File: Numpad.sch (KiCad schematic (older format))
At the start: 7 parts, among them U16 SN74LVC1G04DBVR, U17 74LS597, U18 74LS597, U19 74LS597

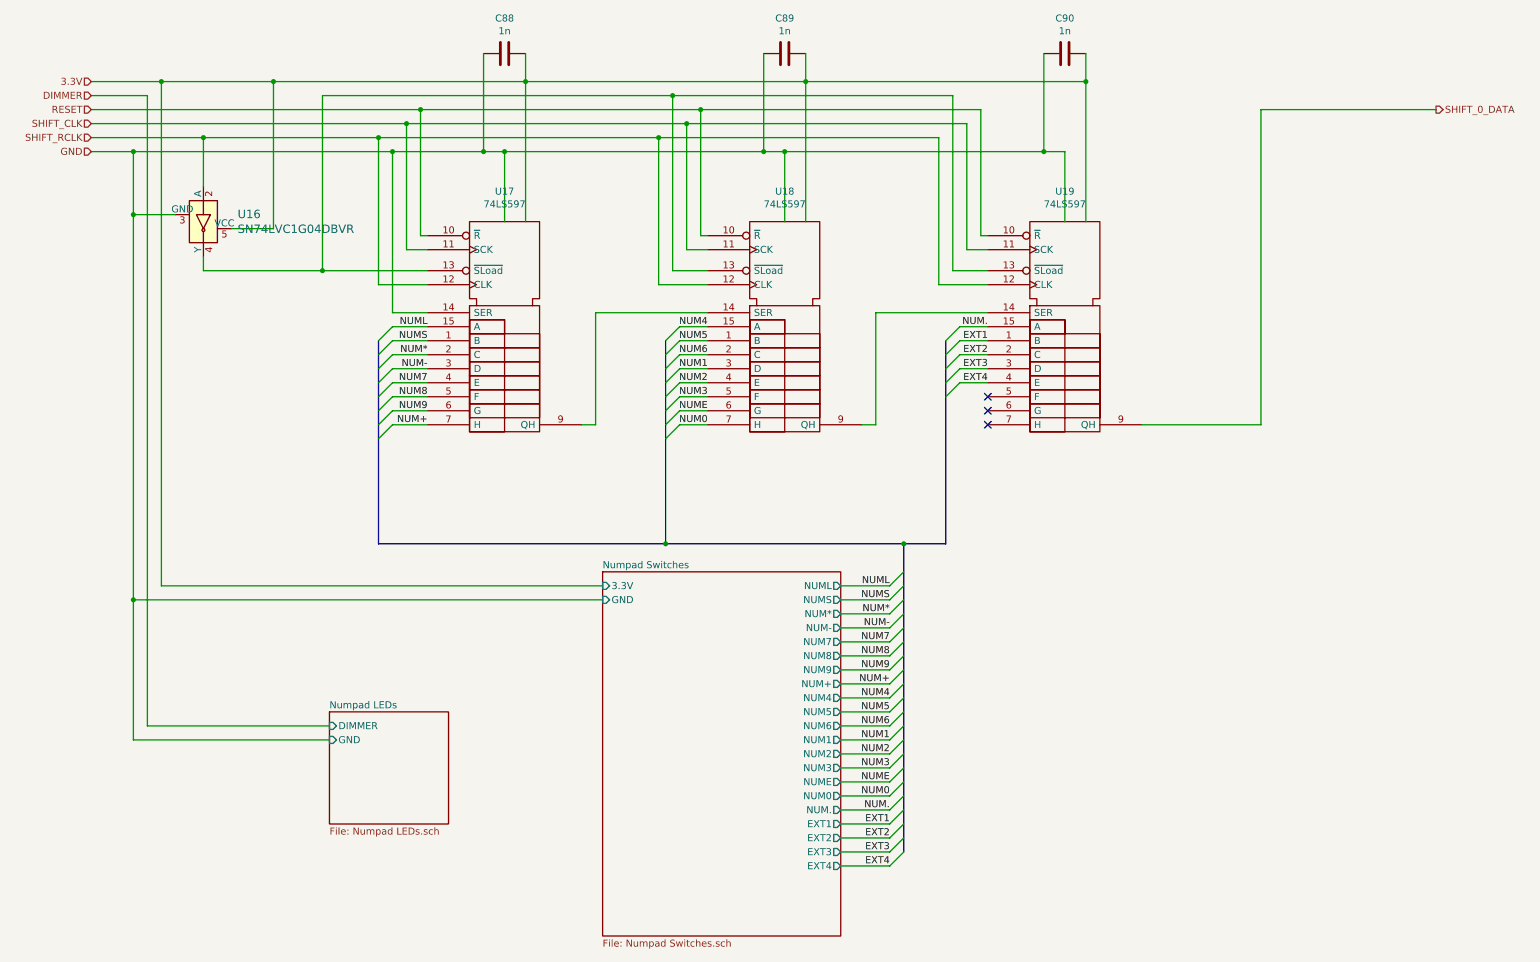
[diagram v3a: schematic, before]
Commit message: Redesigned for single large PCB
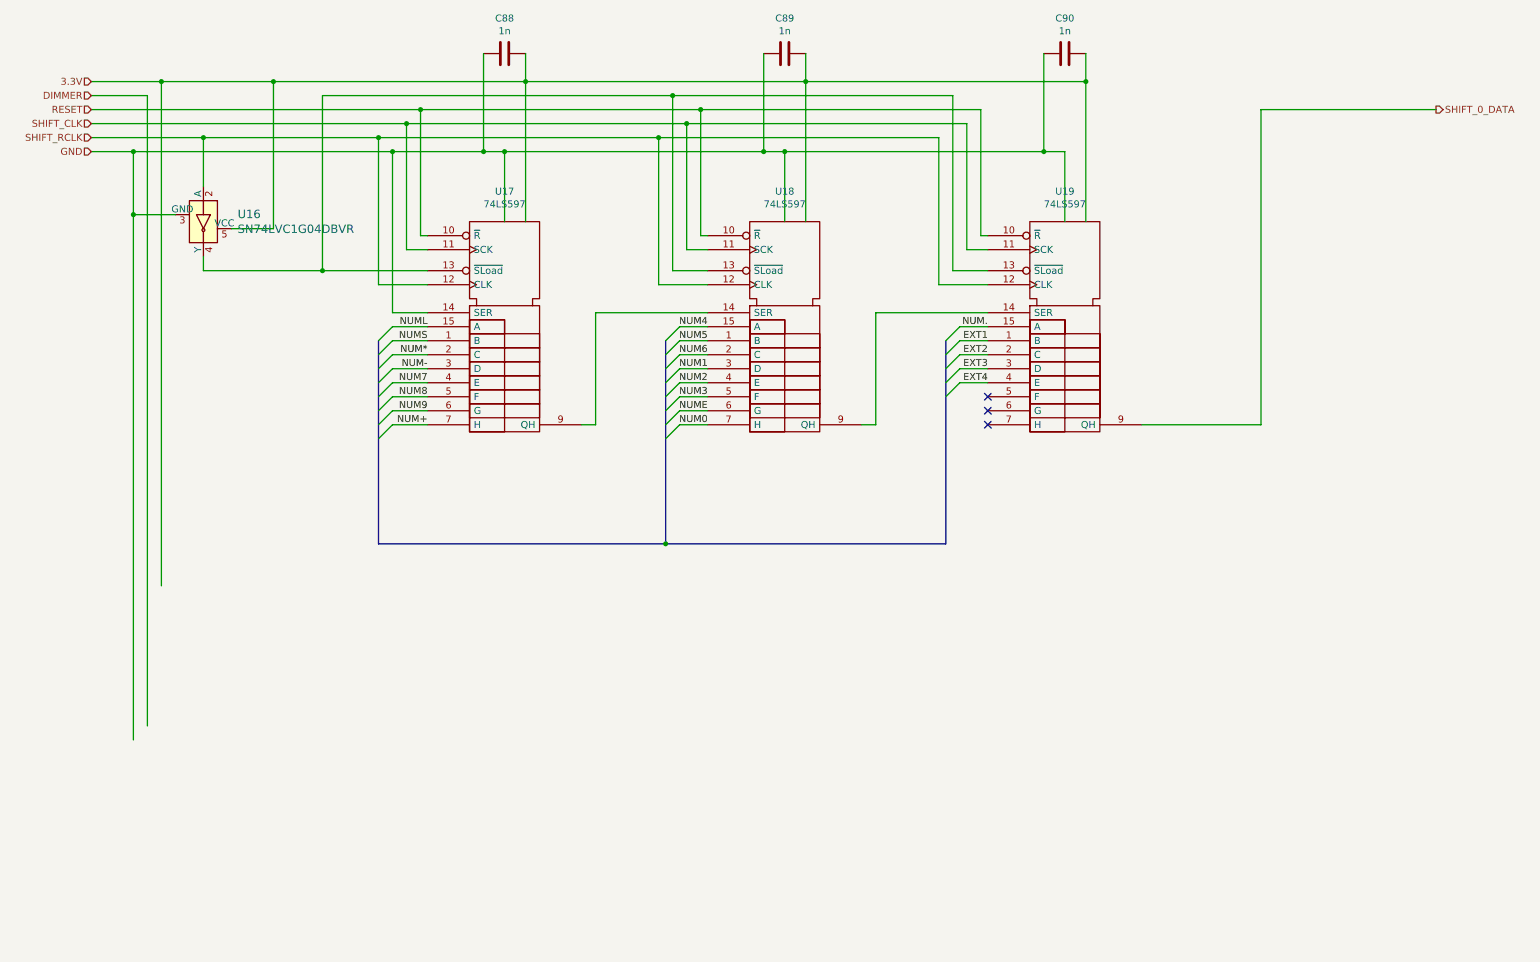
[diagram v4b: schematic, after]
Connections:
- wire segments 130 -> 104
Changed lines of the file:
@@
 $Descr A4 11693 8268
 encoding utf-8
-Sheet 13 18
+Sheet 18 18
 Title ""
 Date ""
@@
 	1400 1200 1400 5700
 Wire Wire Line
-	1400 5700 2700 5700
-Wire Wire Line
 	1500 1100 1500 4700
-Wire Wire Line
-	1300 5800 2700 5800
 Wire Wire Line
 	9350 1300 9350 3550
@@
 Wire Wire Line
 	1300 1600 1300 2050
-Wire Wire Line
-	4650 4800 1300 4800
-Connection ~ 1300 4800
-Wire Wire Line
-	1300 4800 1300 5800
-Wire Wire Line
-	1500 4700 4650 4700
 Wire Wire Line
 	7200 2850 7400 2850
@@
 Entry Wire Line
 	7100 3350 7200 3250
-$Sheet
-S 4650 4600 1700 2600
-U 5E9CBBD2
-F0 "Numpad Switches" 50
-F1 "Numpad Switches.sch" 50
-F2 "3.3V" I L 4650 4700 50
-F3 "GND" I L 4650 4800 50
-F4 "NUML" O R 6350 4700 50
-F5 "NUMS" O R 6350 4800 50
-F6 "NUM*" O R 6350 4900 50
-F7 "NUM-" O R 6350 5000 50
-F8 "NUM7" O R 6350 5100 50
-F9 "NUM8" O R 6350 5200 50
-F10 "NUM9" O R 6350 5300 50
-F11 "NUM+" O R 6350 5400 50
-F12 "NUM4" O R 6350 5500 50
-F13 "NUM5" O R 6350 5600 50
-F14 "NUM6" O R 6350 5700 50
-F15 "NUM1" O R 6350 5800 50
-F16 "NUM2" O R 6350 5900 50
-F17 "NUM3" O R 6350 6000 50
-F18 "NUME" O R 6350 6100 50
-F19 "NUM0" O R 6350 6200 50
-F20 "NUM." O R 6350 6300 50
-F21 "EXT1" O R 6350 6400 50
-F22 "EXT2" O R 6350 6500 50
-F23 "EXT3" O R 6350 6600 50
-F24 "EXT4" O R 6350 6700 50
-$EndSheet
-Wire Wire Line
-	6350 4700 6700 4700
-Wire Wire Line
-	6350 4800 6700 4800
-Wire Wire Line
-	6350 4900 6700 4900
-Wire Wire Line
-	6350 5000 6700 5000
-Wire Wire Line
-	6350 5100 6700 5100
-Wire Wire Line
-	6350 5200 6700 5200
-Wire Wire Line
-	6350 5300 6700 5300
-Wire Wire Line
-	6350 5400 6700 5400
-Wire Wire Line
-	6350 5500 6700 5500
-Wire Wire Line
-	6350 5600 6700 5600
-Wire Wire Line
-	6350 5700 6700 5700
-Wire Wire Line
-	6350 5800 6700 5800
-Wire Wire Line
-	6350 5900 6700 5900
-Wire Wire Line
-	6350 6000 6700 6000
-Wire Wire Line
-	6350 6100 6700 6100
-Wire Wire Line
-	6350 6200 6700 6200
-Wire Wire Line
-	6350 6300 6700 6300
-Wire Wire Line
-	6350 6400 6700 6400
-Wire Wire Line
-	6350 6500 6700 6500
-Wire Wire Line
-	6350 6600 6700 6600
-Wire Wire Line
-	6350 6700 6700 6700
-Text Label 6700 4700 2    50   ~ 0
-NUML
-Text Label 6700 4800 2    50   ~ 0
-NUMS
-Text Label 6700 4900 2    50   ~ 0
-NUM*
-Text Label 6700 5000 2    50   ~ 0
-NUM-
-Text Label 6700 5100 2    50   ~ 0
-NUM7
-Text Label 6700 5200 2    50   ~ 0
-NUM8
-Text Label 6700 5300 2    50   ~ 0
-NUM9
-Text Label 6700 5400 2    50   ~ 0
-NUM+
-Text Label 6700 5500 2    50   ~ 0
-NUM4
-Text Label 6700 5600 2    50   ~ 0
-NUM5
-Text Label 6700 5700 2    50   ~ 0
-NUM6
-Text Label 6700 5800 2    50   ~ 0
-NUM1
-Text Label 6700 5900 2    50   ~ 0
-NUM2
-Text Label 6700 6000 2    50   ~ 0
-NUM3
-Text Label 6700 6100 2    50   ~ 0
-NUME
-Text Label 6700 6200 2    50   ~ 0
-NUM0
-Text Label 6700 6300 2    50   ~ 0
-NUM.
-Text Label 6700 6400 2    50   ~ 0
-EXT1
-Text Label 6700 6500 2    50   ~ 0
-EXT2
-Text Label 6700 6600 2    50   ~ 0
-EXT3
-Text Label 6700 6700 2    50   ~ 0
-EXT4
-Entry Wire Line
-	6700 4700 6800 4600
-Entry Wire Line
-	6700 4800 6800 4700
-Entry Wire Line
-	6700 4900 6800 4800
-Entry Wire Line
-	6700 5000 6800 4900
-Entry Wire Line
-	6700 5100 6800 5000
-Entry Wire Line
-	6700 5200 6800 5100
-Entry Wire Line
-	6700 5300 6800 5200
-Entry Wire Line
-	6700 5400 6800 5300
-Entry Wire Line
-	6700 5500 6800 5400
-Entry Wire Line
-	6700 5600 6800 5500
-Entry Wire Line
-	6700 5700 6800 5600
-Entry Wire Line
-	6700 5800 6800 5700
-Entry Wire Line
-	6700 5900 6800 5800
-Entry Wire Line
-	6700 6000 6800 5900
-Entry Wire Line
-	6700 6100 6800 6000
-Entry Wire Line
-	6700 6200 6800 6100
-Entry Wire Line
-	6700 6300 6800 6200
-Entry Wire Line
-	6700 6400 6800 6300
-Entry Wire Line
-	6700 6500 6800 6400
-Entry Wire Line
-	6700 6600 6800 6500
-Entry Wire Line
-	6700 6700 6800 6600
-Wire Bus Line
-	6800 4400 5100 4400
 Connection ~ 5100 4400
 Wire Bus Line
 	5100 4400 3050 4400
-Wire Bus Line
-	6800 4400 7100 4400
-Connection ~ 6800 4400
-$Sheet
-S 2700 5600 850  800
-U 5EFD9CB6
-F0 "Numpad LEDs" 50
-F1 "Numpad LEDs.sch" 50
-F2 "DIMMER" I L 2700 5700 50
-F3 "GND" I L 2700 5800 50
-$EndSheet
 $Comp
 L dk_Logic-Gates-and-Inverters:SN74LVC1G04DBVR U?
@@
 Connection ~ 1300 2050
 Wire Wire Line
-	1300 2050 1300 4800
-Wire Wire Line
 	1800 1850 1800 1500
 Connection ~ 1800 1500
@@
 NoConn ~ 7400 3450
 NoConn ~ 7400 3550
+Wire Wire Line
+	1300 2050 1300 5800
+Wire Bus Line
+	5100 4400 7100 4400
 Wire Bus Line
 	7100 2950 7100 4400
@@
 Wire Bus Line
 	3050 2950 3050 4400
-Wire Bus Line
-	6800 4400 6800 6600
 $EndSCHEMATC
